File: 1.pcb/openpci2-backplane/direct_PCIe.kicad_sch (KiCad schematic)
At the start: 13 parts, among them J3 BWSMA-KWE-Z001, J5 X3113WVS-64-9TV01, J6 BWSMA-KWE-Z001, J7 AS0BC21-S30BM-7H

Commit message: Kicad library update
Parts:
- J3, J6: footprint PCM_av_lib:BWSMA-KWE-Z001 -> PCM_Chili-chips:BWSMA-KWE-Z001; symbol PCM_BWSMA-KWE-Z001:Conn_Coaxial -> PCM_Chili-chips:Conn_Coaxial
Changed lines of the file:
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@@
 	)
 	(symbol
-		(lib_id "PCM_BWSMA-KWE-Z001:Conn_Coaxial")
+		(lib_id "PCM_Chili-chips:Conn_Coaxial")
 		(at 170.18 138.43 0)
 		(unit 1)
@@
 			)
 		)
-		(property "Footprint" "PCM_av_lib:BWSMA-KWE-Z001"
-			(at 170.18 138.43 0)
+		(property "Footprint" "PCM_Chili-chips:BWSMA-KWE-Z001"
+			(at 170.18 148.59 0)
 			(effects
 				(font
@@
 		)
 		(property "Description" "coaxial connector (BNC, SMA, SMB, SMC, Cinch/RCA, LEMO, ...)"
-			(at 170.18 138.43 0)
+			(at 170.18 146.05 0)
 			(effects
 				(font
@@
 		)
 		(property "LCSC" "C496551"
+			(at 170.18 151.13 0)
+			(show_name yes)
+			(effects
+				(font
+					(size 1.27 1.27)
+				)
+				(hide yes)
+			)
+		)
+		(property "DigiKey" ""
+			(at 170.18 138.43 0)
+			(effects
+				(font
+					(size 1.27 1.27)
+				)
+				(hide yes)
+			)
+		)
+		(property "Mouser" ""
+			(at 170.18 138.43 0)
+			(effects
+				(font
+					(size 1.27 1.27)
+				)
+				(hide yes)
+			)
+		)
+		(property "TME" ""
 			(at 170.18 138.43 0)
 			(effects
@@
 	)
 	(symbol
-		(lib_id "PCM_BWSMA-KWE-Z001:Conn_Coaxial")
+		(lib_id "PCM_Chili-chips:Conn_Coaxial")
 		(at 76.2 138.43 0)
 		(unit 1)
@@
 			)
 		)
-		(property "Footprint" "PCM_av_lib:BWSMA-KWE-Z001"
-			(at 76.2 138.43 0)
+		(property "Footprint" "PCM_Chili-chips:BWSMA-KWE-Z001"
+			(at 76.2 148.59 0)
 			(effects
 				(font
@@
 		)
 		(property "Description" "coaxial connector (BNC, SMA, SMB, SMC, Cinch/RCA, LEMO, ...)"
-			(at 76.2 138.43 0)
+			(at 76.2 146.05 0)
 			(effects
 				(font
@@
 		)
 		(property "LCSC" "C496551"
-			(at 76.2 138.43 0)
-			(effects
-				(font
+			(at 76.2 151.13 0)
+			(show_name yes)
+			(effects
+				(font

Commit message: Final PCB layout revision, ready for manufacturing
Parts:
- J3, J6: footprint PCM_Chili-chips:BWSMA-KWE-Z001 -> PCM_av_lib:BWSMA-KWE-Z001; symbol PCM_Chili-chips:Conn_Coaxial -> PCM_BWSMA-KWE-Z001:Conn_Coaxial
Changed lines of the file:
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@@
 	)
 	(symbol
-		(lib_id "PCM_Chili-chips:Conn_Coaxial")
+		(lib_id "PCM_BWSMA-KWE-Z001:Conn_Coaxial")
 		(at 170.18 138.43 0)
 		(unit 1)
@@
 			)
 		)
-		(property "Footprint" "PCM_Chili-chips:BWSMA-KWE-Z001"
-			(at 170.18 148.59 0)
+		(property "Footprint" "PCM_av_lib:BWSMA-KWE-Z001"
+			(at 170.18 138.43 0)
 			(effects
 				(font
@@
 		)
 		(property "Description" "coaxial connector (BNC, SMA, SMB, SMC, Cinch/RCA, LEMO, ...)"
-			(at 170.18 146.05 0)
+			(at 170.18 138.43 0)
 			(effects
 				(font
@@
 		)
 		(property "LCSC" "C496551"
-			(at 170.18 151.13 0)
-			(show_name yes)
-			(effects
-				(font
-					(size 1.27 1.27)
-				)
-				(hide yes)
-			)
-		)
-		(property "DigiKey" ""
-			(at 170.18 138.43 0)
-			(effects
-				(font
-					(size 1.27 1.27)
-				)
-				(hide yes)
-			)
-		)
-		(property "Mouser" ""
-			(at 170.18 138.43 0)
-			(effects
-				(font
-					(size 1.27 1.27)
-				)
-				(hide yes)
-			)
-		)
-		(property "TME" ""
 			(at 170.18 138.43 0)
 			(effects
@@
 	)
 	(symbol
-		(lib_id "PCM_Chili-chips:Conn_Coaxial")
+		(lib_id "PCM_BWSMA-KWE-Z001:Conn_Coaxial")
 		(at 76.2 138.43 0)
 		(unit 1)
@@
 			)
 		)
-		(property "Footprint" "PCM_Chili-chips:BWSMA-KWE-Z001"
-			(at 76.2 148.59 0)
+		(property "Footprint" "PCM_av_lib:BWSMA-KWE-Z001"
+			(at 76.2 138.43 0)
 			(effects
 				(font
@@
 		)
 		(property "Description" "coaxial connector (BNC, SMA, SMB, SMC, Cinch/RCA, LEMO, ...)"
-			(at 76.2 146.05 0)
+			(at 76.2 138.43 0)
 			(effects
 				(font
@@
 		)
 		(property "LCSC" "C496551"
-			(at 76.2 151.13 0)
-			(show_name yes)
-			(effects
-				(font
+			(at 76.2 138.43 0)
+			(effects
+				(font

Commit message: Update schematic and PCB layout design
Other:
- company: Chili.CHIPS*ba -> COPYRIGHT (C) Chili.CHIPS.ba doo
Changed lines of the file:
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@@
 		(date "2025-10-21")
 		(rev "r1B1")
-		(company "Chili.CHIPS*ba")
+		(company "COPYRIGHT (C) Chili.CHIPS.ba doo")
+		(comment 1 "https://cern-ohl.web.cern.ch")
+		(comment 2 "Licensed under CERN-OHL-P v2")
 	)
 	(text "RC4\n"

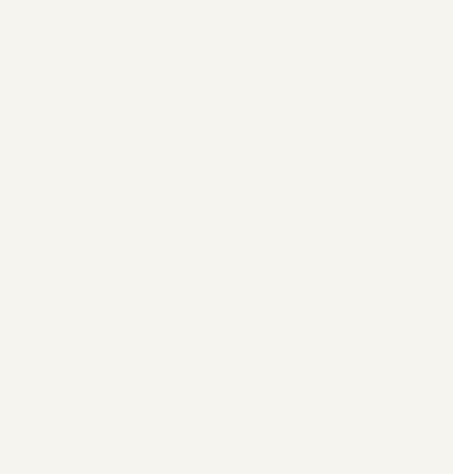
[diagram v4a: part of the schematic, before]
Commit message: Complete rev.B PCB layout for manufacturing
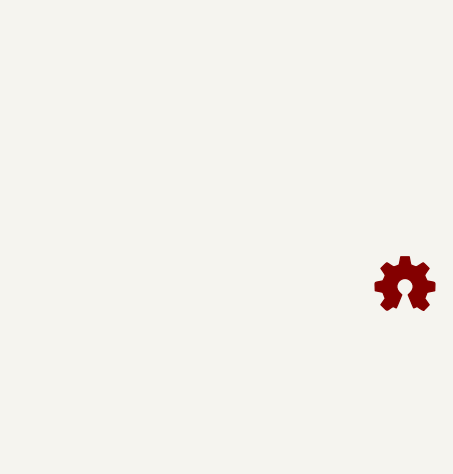
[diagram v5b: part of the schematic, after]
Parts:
- added LOGO5: Open hardware logo, PCM_EEZ_unsorted:Open HW logo, symbol PCM_EEZ_symbols:Open HW logo
